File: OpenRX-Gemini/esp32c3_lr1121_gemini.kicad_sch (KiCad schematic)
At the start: 65 parts, among them T1 0900PC16J0042001E, T2 0900PC16J0042001E, U1 ESP32-C3FH4, U10 RFX2401C, U11 SKY13588-460LF, U2 TLV75533PDQNR, U3 TS2306A 240GF MSM 9_C2976675, U4 LR1121IMLTRT, U5 OW7EL89CENUYO3YLC-32M, U6 SKY13588-460LF, U7 RFX2401C, U8 OW7EL89CENUYO3YLC-32M, U9 LR1121IMLTRT, X1 CJ17-400001010B20

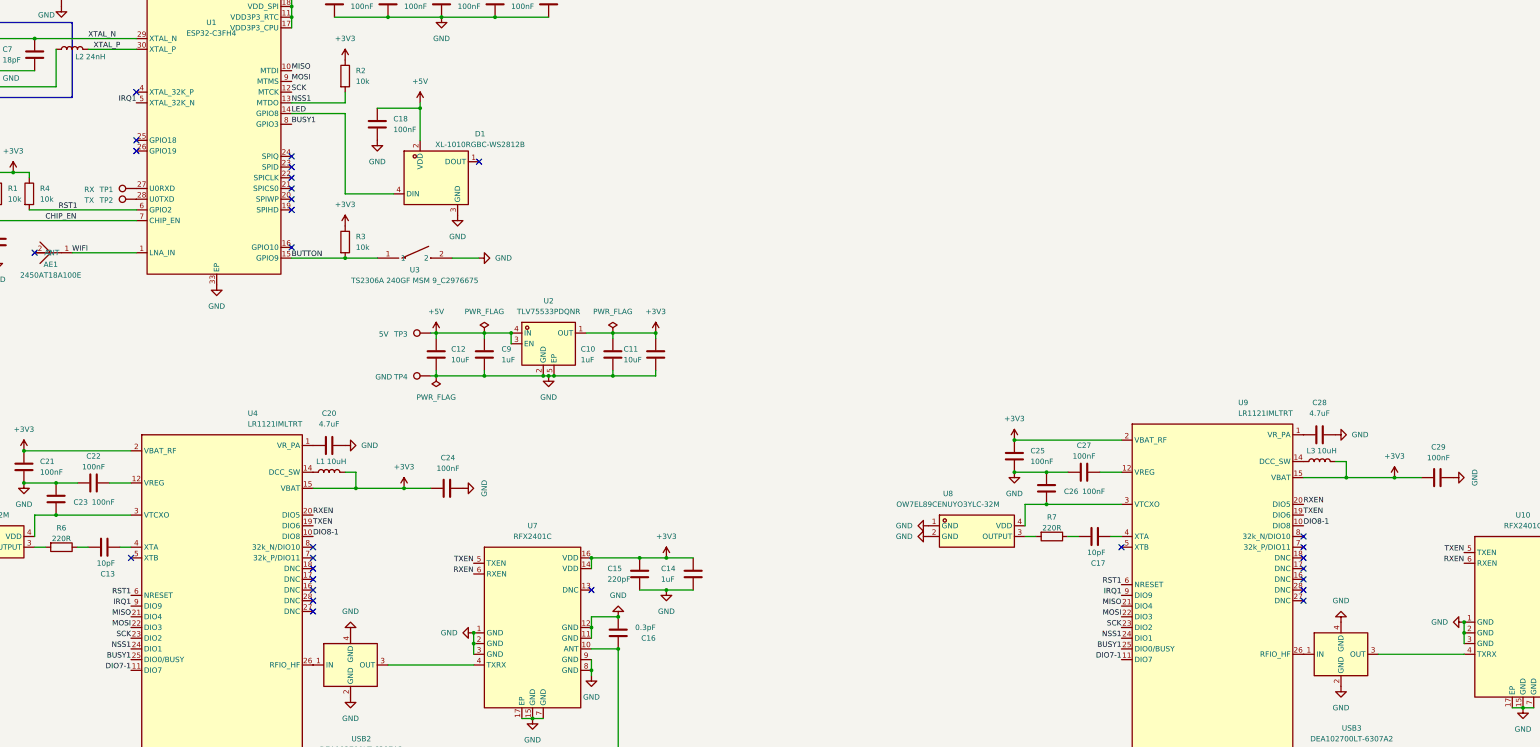
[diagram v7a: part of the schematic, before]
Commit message: Apply JLCPCB 6-layer advanced DRC rules to Mono and Gemini
Rules applied:
- Min clearance: 0.09mm (3.5mil)
- Min track width: 0.09mm (3.5mil)
- Min via diameter: 0.25mm
- Min via drill: 0.15mm
- Min annular ring: 0.05mm
- Min hole-to-hole: 0.25mm
- Default net class clearance: 0.09mm (was 0.2mm — this was the override)
- Default track width: 0.1mm
- Zone clearance: 0.09mm (was 0.5mm)
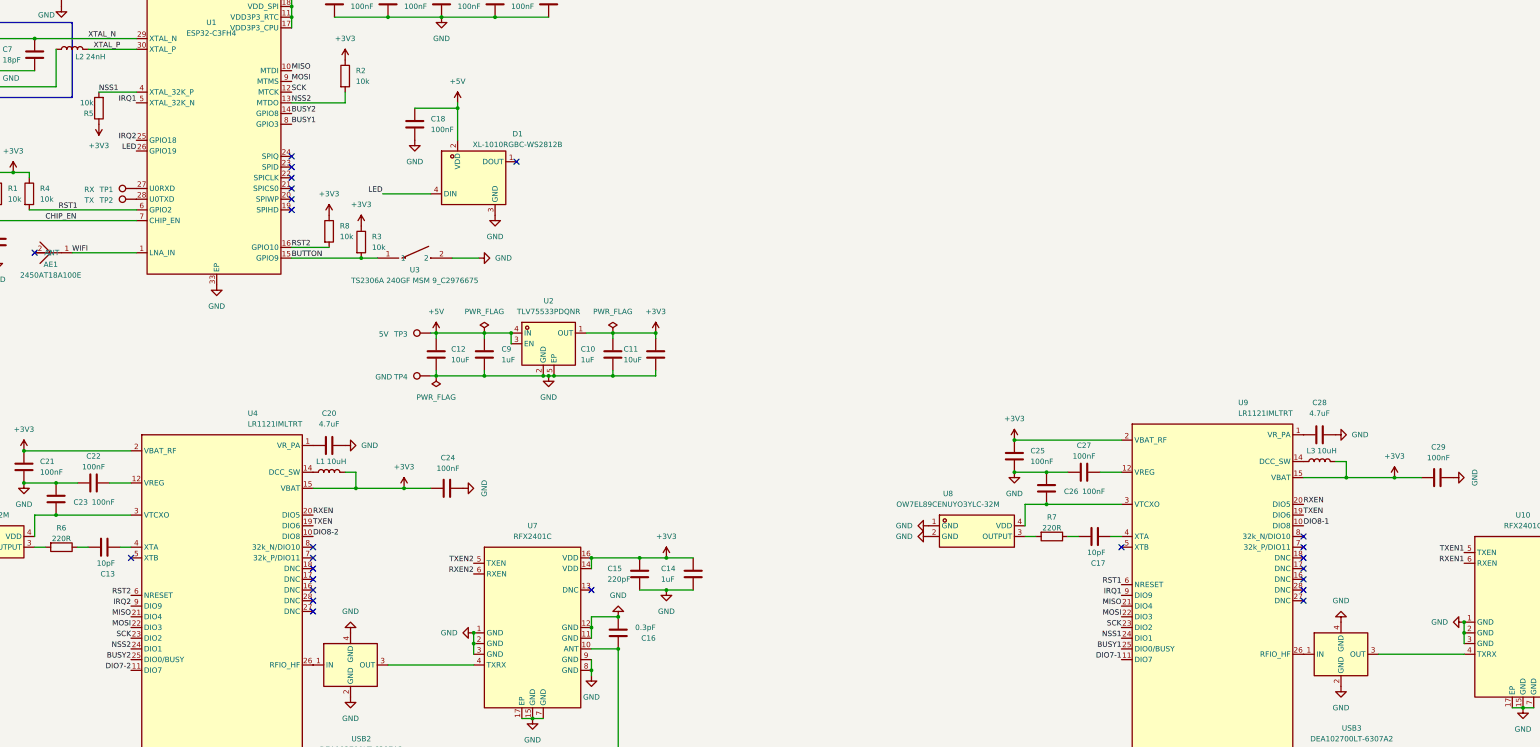
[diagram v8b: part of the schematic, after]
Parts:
- added R5, R8: 10k, Resistor_SMD:R_0201_0603Metric, symbol Device:R
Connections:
- net +3V3: now also R5.1, R8.1
- net BUSY1: no longer U4.25 (DIO0/BUSY)
- net DIO7-1: no longer U4.11 (DIO7)
- net DIO8-1: no longer U4.10 (DIO8)
- net IRQ1: no longer U4.9 (DIO9)
- net LED: now also U1.26 (GPIO19); no longer U1.14 (GPIO8)
- net NSS1: now also U1.4 (XTAL_32K_P), R5.2; no longer R2.2, U1.13 (MTDO), U4.24 (DIO1)
- net RST1: no longer U4.6 (NRESET)
- net RXEN: no longer U10.6 (RXEN), U7.6 (RXEN)
- net TXEN: no longer U10.5 (TXEN), U7.5 (TXEN)
- net RST2: now reaches U1.16 (GPIO10)
- net RST2: now also U4.6 (NRESET), R8.2
- net IRQ2: now reaches U1.25 (GPIO18)
- net IRQ2: now also U4.9 (DIO9)
- new net BUSY2: U1.14 (GPIO8), U4.25 (DIO0/BUSY)
- new net DIO7-2: U4.11 (DIO7)
- new net DIO8-2: U4.10 (DIO8)
- new net NSS2: R2.2, U1.13 (MTDO), U4.24 (DIO1)
- new net RXEN1: U10.6 (RXEN)
- new net RXEN2: U7.6 (RXEN)
- new net TXEN1: U10.5 (TXEN)
- new net TXEN2: U7.5 (TXEN)
- no-connect marks 32 -> 28
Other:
- moved on the sheet: C18, D1, R3
